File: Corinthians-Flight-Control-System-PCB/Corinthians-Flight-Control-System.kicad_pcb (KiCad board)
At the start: 4 copper layers, 48.9 x 72.5 mm, 81 parts, among them J0 RaspberryPi, J1 50ohm Coaxial Ant, J10 M8, J11 M9, J12 M10, J2 GPS/Compass, J3 M1, J4 M2, J5 M3, J6 M4, J7 M5, J8 M6, J9 M7, SW1 BootSW, SW2 SW_DIP_x01, SW3 SW_s, U1 STM32F103C8Tx, U2 LSM6DS3, U3 BMP280, U4 NRF24L01, U5 IST8310, U6 AMS1117-3.3, U7 AMS1117-5.0, Y1 8Mhz, Y2 16Mhz

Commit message: New corrections and CAD files
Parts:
- F1: value 500mA -> 3A
- moved H1 1.18 mm to (102.0, 135.5)
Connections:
- U1 pad 14: CE -> Net-(U1-Pad14)
- U1 pad 15: CSN -> SCK
- U1 pad 16: Net-(U1-Pad16) -> MISO
- U1 pad 17: Net-(U1-Pad17) -> MOSI
- U1 pad 18: Net-(U1-Pad18) -> PWM1-G
- U1 pad 26: PWM1-E -> CE
- U1 pad 27: PWM1-F -> CSN
- U1 pad 28: PWM1-G -> SW_s
- U1 pad 39: SCK -> Net-(U1-Pad39)
- U1 pad 40: MISO -> PWM1-E
- U1 pad 41: MOSI -> PWM1-F
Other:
- net class Default: trace_width 0.25 -> 0.32; via_dia 0.8 -> 0.62
- net class Power added: clearance 0.5, trace_width 0.5, via_dia 0.8, via_drill 0.4

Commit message: updates
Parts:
- removed R15: 10K, Resistor_SMD:R_0402_1005Metric
- added C30: 0.1uF, Capacitor_SMD:C_0402_1005Metric, F.Cu at (110.4, 151.9)
- C10, C11, C19, C20: footprint Capacitor_SMD:C_0603_1608Metric -> Capacitor_SMD:C_0805_2012Metric
- moved C10 4.14 mm to (113.3, 132.3)
- moved C11 3.63 mm to (117.6, 132.3), turned to 0 degrees
- moved C20 0.75 mm to (126.8, 123.0)
- moved C19 0.57 mm to (122.3, 123.0)
- renumbered R14 to R10, R16 to R11, R17 to R12
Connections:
- SW2 pad 1: Net-(R15-Pad2) -> GND

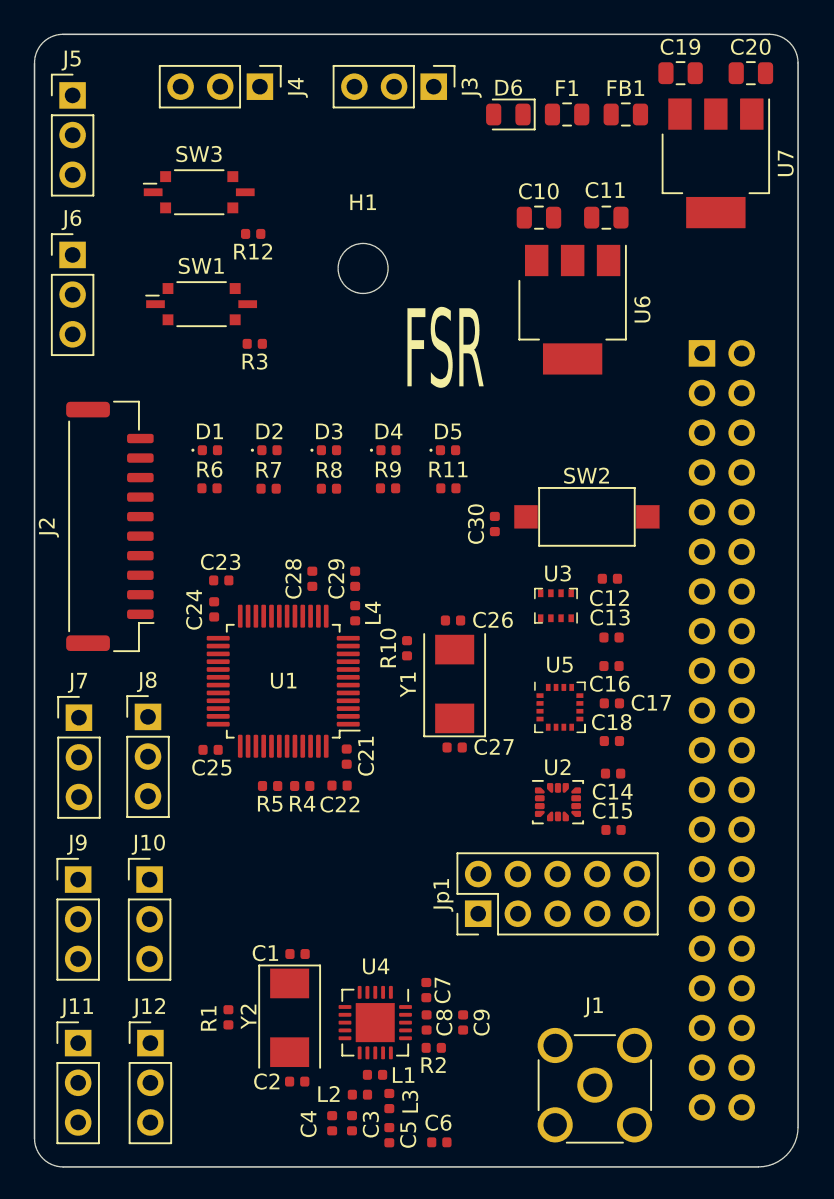
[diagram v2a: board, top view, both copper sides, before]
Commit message: schematic and pcb routing update
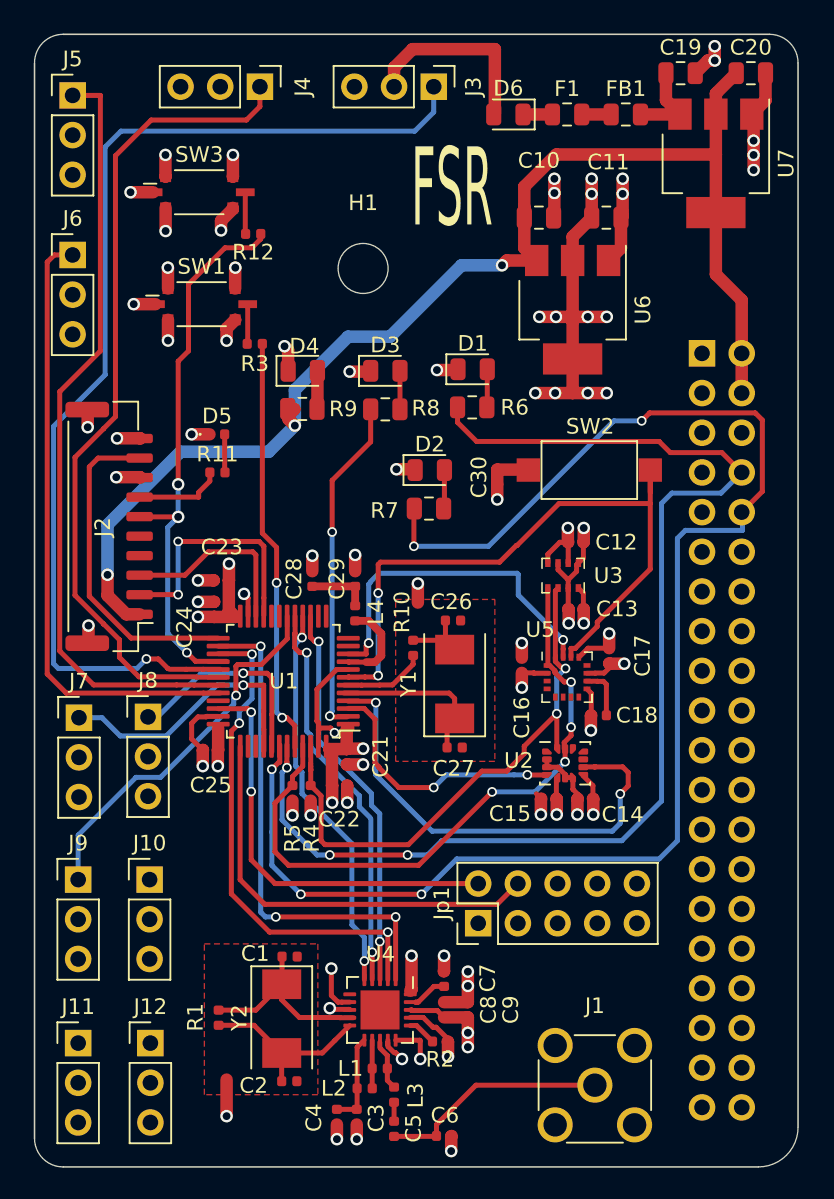
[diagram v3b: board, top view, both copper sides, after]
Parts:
- D1, D2, D3, D4: footprint LED_SMD:LED_0402_1005Metric -> LED_SMD:LED_0805_2012Metric
- R6, R7, R8, R9: footprint Resistor_SMD:R_0402_1005Metric -> Resistor_SMD:R_0805_2012Metric
- moved D1 17.6 mm to (109.0, 142.0)
- moved R6 17.6 mm to (109.0, 144.4)
- moved R11 14.8 mm to (92.7, 148.6)
- moved D5 14.8 mm to (92.7, 146.2)
- moved D2 10.3 mm to (106.3, 148.4)
- moved R7 10.3 mm to (106.2, 150.9)
- moved D4 7.48 mm to (98.1, 142.1)
- moved R9 7.48 mm to (98.1, 144.5)
- moved R8 6.23 mm to (103.4, 144.6)
- moved D3 6.23 mm to (103.4, 142.1)
- moved C16 5.74 mm to (112.2, 160.9), turned to 270 degrees
- moved C15 4.60 mm to (113.9, 169.5)
- moved C12 3.20 mm to (115.6, 153.1)
- moved C17 3.05 mm to (117.8, 160.3), turned to 90 degrees
- moved C30 3.00 mm to (110.6, 148.9)
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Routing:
- net GND: track 0.00 -> 104.9 mm, vias 0 -> 54
- net TX: track 0.00 -> 96.0 mm, vias 0 -> 5
- net +5VD: track 0.00 -> 84.8 mm, vias 0 -> 3
- net +3V3: track 0.00 -> 78.0 mm, vias 0 -> 30
- net RX: track 0.00 -> 77.1 mm, vias 0 -> 3
- net PWM1-A: track 0.00 -> 69.2 mm, vias 0 -> 1
- net PWM1-B: track 0.00 -> 54.3 mm
- net PWM1-C: track 0.00 -> 49.8 mm
- net NRST: track 0.00 -> 43.7 mm, vias 0 -> 2
- net SCL: track 0.00 -> 41.6 mm, vias 0 -> 4
- net PWM1-D: track 0.00 -> 39.8 mm
- net SDA: track 0.00 -> 36.6 mm, vias 0 -> 2
- net SW_s: track 0.00 -> 36.1 mm, vias 0 -> 3
- net CE: track 0.00 -> 32.5 mm, vias 0 -> 3
- net CSN: track 0.00 -> 32.1 mm, vias 0 -> 3
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- added copper zone on Power_3.3v.Cu, net +3V3
- added copper zone on F.Cu, net GND
- added copper zone on Power_GND.Cu, net GND
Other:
- net class Power: trace_width 0.5 -> 0.8; via_drill 0.4 -> 0.5
- net class ic added: clearance 0, trace_width 0.32, via_dia 0.62, via_drill 0.4

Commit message: Routing finished ?
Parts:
- moved C28 1.23 mm to (98.9, 154.2)
- moved C29 1.22 mm to (101.5, 154.2)
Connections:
- C11 pad 1: +3V3 -> +3.3VA
- C12 pad 2: +3V3 -> +3.3VA
- C13 pad 1: +3V3 -> +3.3VA
- C14 pad 1: +3V3 -> +3.3VA
- C15 pad 1: +3V3 -> +3.3VA
- C16 pad 2: +3V3 -> +3.3VA
- C17 pad 2: +3V3 -> +3.3VA
- C21 pad 2: +3V3 -> +3.3VA
- C22 pad 2: +3V3 -> +3.3VA
- C23 pad 2: +3V3 -> +3.3VA
- C24 pad 2: +3V3 -> +3.3VA
- C25 pad 2: +3V3 -> +3.3VA
- C8 pad 2: +3V3 -> +3.3VA
- C9 pad 2: +3V3 -> +3.3VA
- J2 pad 8: +3V3 -> +3.3VA
- Jp1 pad 1: +3V3 -> +3.3VA
- R4 pad 1: +3V3 -> +3.3VA
- R5 pad 1: +3V3 -> +3.3VA
- SW1 pad 1: +3V3 -> +3.3VA
- SW3 pad 1: +3V3 -> +3.3VA
- U1 pad 1: +3V3 -> +3.3VA
- U1 pad 24: +3V3 -> +3.3VA
- U1 pad 36: +3V3 -> +3.3VA
- U1 pad 48: +3V3 -> +3.3VA
- U2 pad 5: +3V3 -> +3.3VA
- U2 pad 8: +3V3 -> +3.3VA
- U3 pad 2: +3V3 -> +3.3VA
- U3 pad 6: +3V3 -> +3.3VA
- U3 pad 8: +3V3 -> +3.3VA
- U4 pad 15: +3V3 -> +3.3VA
- U4 pad 18: +3V3 -> +3.3VA
- U4 pad 7: +3V3 -> +3.3VA
- U5 pad 13: +3V3 -> +3.3VA
- U5 pad 2: +3V3 -> +3.3VA
- U6 pad 2: +3V3 -> +3.3VA
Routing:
- net +3.3VA: track 5.73 -> 85.9 mm, vias 0 -> 31
- net +3V3: track 78.0 -> 0.00 mm, vias 30 -> 0
- net PWM2-B: track 0.00 -> 73.1 mm, vias 0 -> 4
- net PWM2-C: track 0.00 -> 67.6 mm, vias 0 -> 4
- net PWM2-A: track 0.00 -> 58.5 mm, vias 0 -> 4
- net SDA: track 36.6 -> 62.4 mm, vias 2 -> 4
- net SCL: track 41.6 -> 65.7 mm, vias 4 -> 6
- net GND: track 104.9 -> 102.4 mm, vias 54 -> 55
- net BOOT0: track 26.9 -> 29.4 mm
- net INT_C: track 22.1 -> 23.3 mm
- net INT_IMU2: track 30.6 -> 29.5 mm
- net Net-(C28-Pad1): track 3.98 -> 5.05 mm
- net +5VD: track 84.8 -> 85.8 mm
- net PWM1-B: track 54.3 -> 53.7 mm
- net TX2: track 15.9 -> 15.2 mm
- added copper zone on Power_3.3v.Cu, net +3.3VA
- removed copper zone on Power_3.3v.Cu, net +3V3
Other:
- net class Default: clearance 0.2 -> 0.15
- rule trace_clearance: 0.2 -> 0.15

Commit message: DRC Check
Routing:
- net CSN: track 32.1 -> 36.2 mm, vias 3 -> 2
- net CE: track 32.5 -> 35.6 mm, vias 3 -> 2
- net SCL: track 65.7 -> 63.0 mm
- net TX: track 96.0 -> 93.9 mm
- net GND: track 102.4 -> 100.5 mm
- net SDA: track 62.4 -> 60.9 mm
- net SWDCLK: track 27.5 -> 28.6 mm
- net PWM2-C: track 67.6 -> 68.5 mm
- net Net-(C1-Pad2): track 12.7 -> 13.6 mm
- net SW_s: track 36.3 -> 35.6 mm
- net BOOT0: track 29.4 -> 28.7 mm

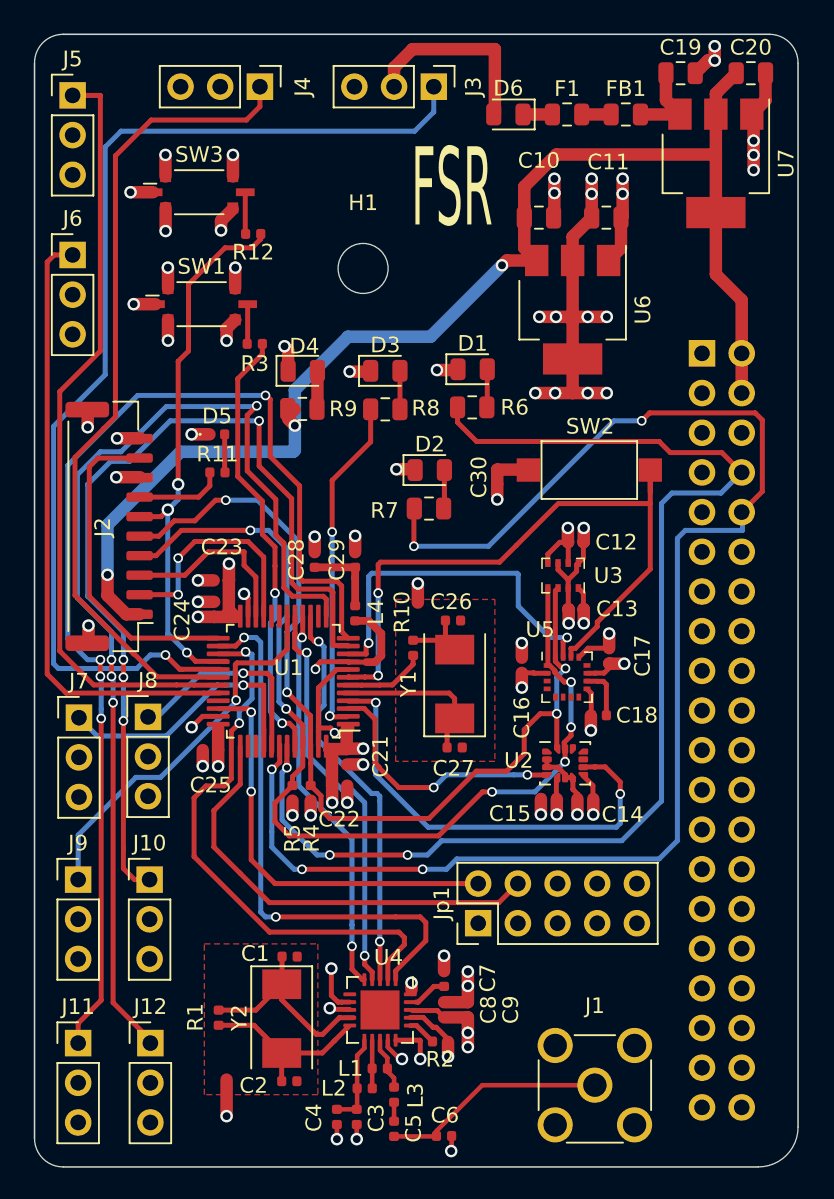
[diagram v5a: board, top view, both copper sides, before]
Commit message: Logo Footprints Added
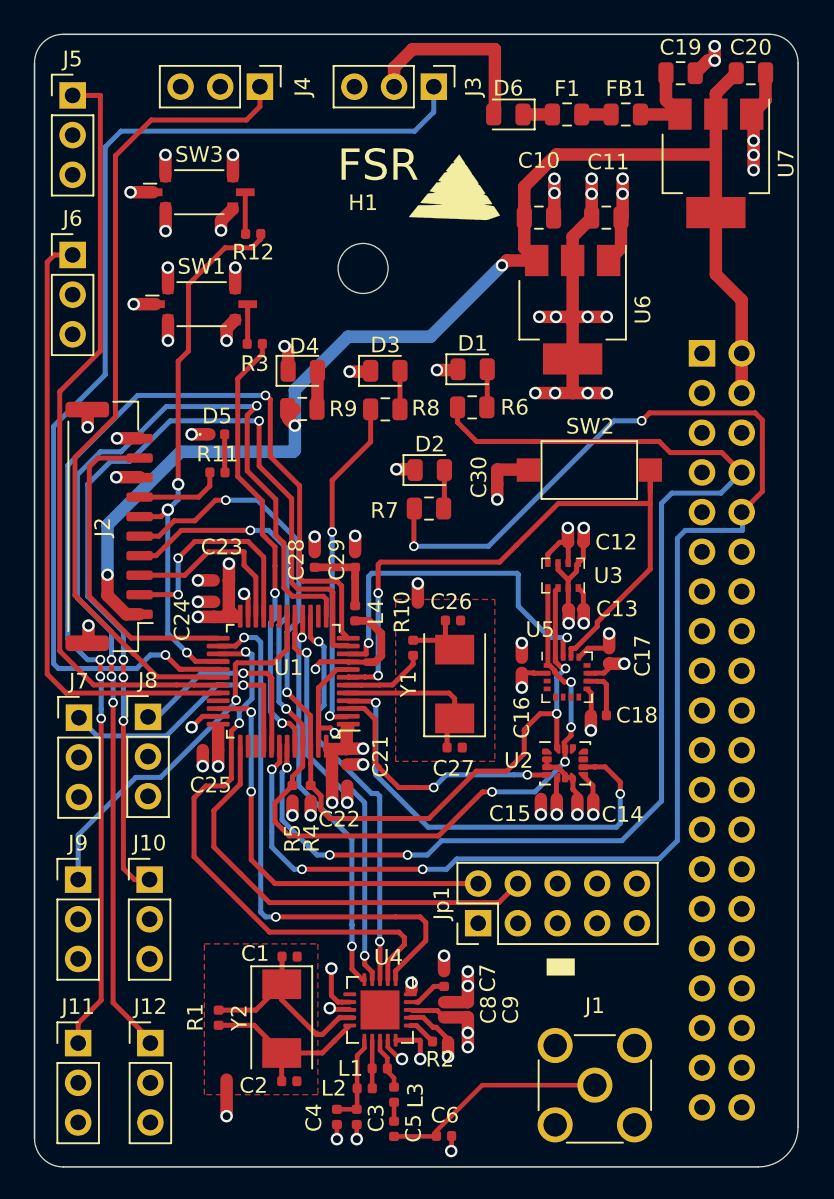
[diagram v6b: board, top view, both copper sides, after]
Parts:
- added ?: LOGO, Logos:pcbLogoFull, B.Cu at (92.7, 158.6)
- added G***: LOGO, Logos:pcbLogo, F.Cu at (107.8, 130.4)
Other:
- board text added: "-"

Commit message: 0402 components changed to 0805
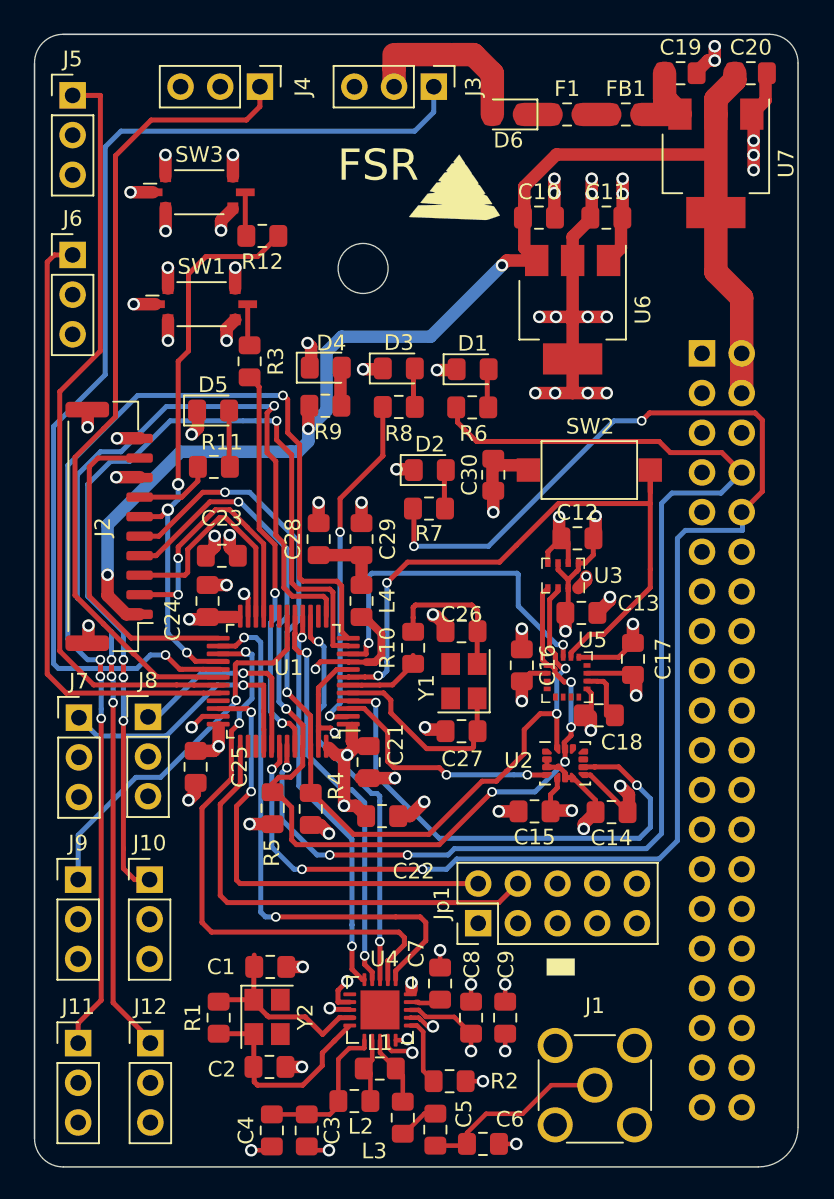
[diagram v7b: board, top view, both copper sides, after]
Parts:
- C1, C12, C13, C14, C15, C16, C17, C18, C2, C21, C22, C23, C24, C25, C26, C27, C28, C29, C3, C30, C4, C5, C6, C7, C8, C9: footprint Capacitor_SMD:C_0402_1005Metric -> Capacitor_SMD:C_0805_2012Metric_Pad1.15x1.40mm_HandSolder
- C10, C11, C19, C20: footprint Capacitor_SMD:C_0805_2012Metric -> Capacitor_SMD:C_0805_2012Metric_Pad1.15x1.40mm_HandSolder
- D1, D2, D3, D4: footprint LED_SMD:LED_0805_2012Metric -> LED_SMD:LED_0805_2012Metric_Pad1.15x1.40mm_HandSolder
- D5: footprint LED_SMD:LED_0402_1005Metric -> LED_SMD:LED_0805_2012Metric_Pad1.15x1.40mm_HandSolder
- D6: footprint Diode_SMD:D_0805_2012Metric -> Diode_SMD:D_0805_2012Metric_Pad1.15x1.40mm_HandSolder
- F1: footprint Fuse:Fuse_0805_2012Metric -> Fuse:Fuse_0805_2012Metric_Pad1.15x1.40mm_HandSolder
- FB1: footprint Inductor_SMD:L_0805_2012Metric -> Inductor_SMD:L_0805_2012Metric_Pad1.15x1.40mm_HandSolder
- L1, L2, L3, L4: footprint Inductor_SMD:L_0402_1005Metric -> Inductor_SMD:L_0805_2012Metric_Pad1.15x1.40mm_HandSolder
- R1, R10, R11, R12, R2, R3, R4, R5: footprint Resistor_SMD:R_0402_1005Metric -> Resistor_SMD:R_0805_2012Metric_Pad1.15x1.40mm_HandSolder
- R6, R7, R8, R9: footprint Resistor_SMD:R_0805_2012Metric -> Resistor_SMD:R_0805_2012Metric_Pad1.15x1.40mm_HandSolder
- Y1, Y2: footprint Crystal:Crystal_SMD_0603-2Pin_6.0x3.5mm -> Crystal:Crystal_SMD_Abracon_ABM8G-4Pin_3.2x2.5mm
- moved C4 4.25 mm to (96.2, 190.7)
- moved C22 3.35 mm to (103.2, 170.6)
- moved C3 3.31 mm to (98.4, 190.7)
- moved C5 2.64 mm to (106.6, 190.7)
- moved R2 2.61 mm to (107.5, 187.6)
- moved C6 2.54 mm to (109.7, 191.6)
- moved C9 2.44 mm to (111.1, 183.5)
- moved C14 1.89 mm to (117.9, 170.3)
- moved C8 1.80 mm to (108.9, 183.5)
- moved R5 1.60 mm to (96.2, 170.1)
- moved C23 1.58 mm to (93.0, 153.9)
- moved L3 1.58 mm to (104.5, 189.9)
- moved C2 1.56 mm to (96.0, 186.6)
- moved D5 1.55 mm to (92.4, 144.6)
- moved C17 1.54 mm to (119.3, 160.5)
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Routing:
- net GND: track 100.5 -> 112.7 mm, vias 55 -> 59
- net +3.3VA: track 85.8 -> 94.4 mm
- net Net-(C3-Pad2): track 5.90 -> 9.95 mm
- net INT_IMU2: track 29.3 -> 33.1 mm
- net Net-(C26-Pad1): track 5.82 -> 9.33 mm
- net RX2: track 11.7 -> 15.0 mm
- net SCL: track 63.0 -> 66.1 mm
- net BOOT0: track 28.7 -> 25.6 mm
- net Net-(C27-Pad2): track 10.6 -> 13.2 mm
- net TX2: track 14.9 -> 17.5 mm
- net Net-(R2-Pad1): track 1.85 -> 4.43 mm
- net Net-(C5-Pad2): track 14.4 -> 12.2 mm
- net SWDIO: track 26.9 -> 29.0 mm
- net Net-(D5-Pad2): track 2.45 -> 4.46 mm
- net Net-(C2-Pad1): track 11.7 -> 13.6 mm
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- removed copper zone on F.Cu, net GND

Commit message: Post DRC Check
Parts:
- moved C18 1.72 mm to (118.7, 164.7)
- moved D6 0.72 mm to (110.6, 125.8)
- moved F1 0.42 mm to (114.7, 125.8)
- moved FB1 0.14 mm to (118.7, 125.8)
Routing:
- net +5V: track 11.2 -> 9.07 mm
- net Net-(C18-Pad2): track 3.26 -> 4.55 mm
- net GND: track 112.7 -> 113.8 mm
- net Net-(C26-Pad1): track 9.33 -> 9.93 mm
